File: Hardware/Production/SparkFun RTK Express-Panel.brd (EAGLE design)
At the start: 219.3 x 141.9 mm, 489 parts, among them J13 Internal, J16 microSD, J17 Qwiic Right Angle, J19 FPC_12_0.5MM_BACKFLIP, J20 External, J21 USB Female Type C Connector, J24 USB Female Type C Connector, J3 USB Female Type C Connector, J31 microSD, J33 Qwiic Right Angle, J34 Internal, J37 FPC_12_0.5MM_BACKFLIP, J39 External, J4 External, J40 USB Female Type C Connector, J43 USB Female Type C Connector, J5 USB Female Type C Connector, J50 microSD, J52 Qwiic Right Angle, J53 Internal, J56 FPC_12_0.5MM_BACKFLIP, Q1 SIL2308-TP, Q2 MBT3904DW1T1, Q3 MBT3904DW1T1, Q4 SIL2308-TP, Q5 MBT3904DW1T1, Q6 SIL2308-TP, U1 74HC4052D, U10 MCP73833, U11 CH340C, U12 MAX17048, U13 LIS2DH12, U14 ADP160, U15 MCP73833, U16 74HC4052D, U17 LIS2DH12, U18 ESP-WROOM-3232D-NARROW, U19 AP2112K-3.3, U2 AP2112K-3.3, U20 U-BLOX_ZED-F9P, U21 CH340C, U22 MAX17048, U23 ADP160, U24 MCP73833, U25 74HC4052D, U26 LIS2DH12, U27 ESP-WROOM-3232D-NARROW, U3 U-BLOX_ZED-F9P, U4 ADP160, U5 ESP-WROOM-3232D-NARROW, U6 CH340C, U7 MAX17048, U8 AP2112K-3.3, U9 U-BLOX_ZED-F9P

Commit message: Update v12 panel files.
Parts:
- added D19: 250mA/100V, SparkFun-DiscreteSemi:SOD-323
- added D20: 3A/10V/280mV, SparkFun-DiscreteSemi:SOD-323
- added D21: PESD0402, New_Parts:0402
- added U$184: (no value), output:L1#L20
- added U$185: (no value), output:ACTIVE1
- added U$186: (no value), output:ANTENNA2
- D10: value PRTR5V0U2F -> PESD0402; device SparkFun-IC-Power:SOT886 -> New_Parts:0402
- D11: value 250mA/100V -> PRTR5V0U2F; device SparkFun-DiscreteSemi:SOD-323 -> SparkFun-IC-Power:SOT886
- D12: value 3A/10V/280mV -> 250mA/100V
- D13, D16: value PRTR5V0U2F -> 3A/10V/280mV; device SparkFun-IC-Power:SOT886 -> SparkFun-DiscreteSemi:SOD-323
- D14: value 3A/10V/280mV -> PESD0402; device SparkFun-DiscreteSemi:SOD-323 -> New_Parts:0402
- D15, D18: value 3A/10V/280mV -> PRTR5V0U2F; device SparkFun-DiscreteSemi:SOD-323 -> SparkFun-IC-Power:SOT886
- D17: value 250mA/100V -> 3A/10V/280mV
- J19: value FPC_12_0.5MM_BACKFLIP -> External; device RTK Facet:FPC_12_DOUBLESIDED_BACKFLIP -> SparkFun-Connectors:JST04_1MM_RA
- J20: value External -> FPC_12_0.5MM_BACKFLIP; device SparkFun-Connectors:JST04_1MM_RA -> RTK Facet:FPC_12_DOUBLESIDED_BACKFLIP
- J37, J56: value FPC_12_0.5MM_BACKFLIP -> (none); device RTK Facet:FPC_12_DOUBLESIDED_BACKFLIP -> SparkFun-Connectors:1X01_NO_SILK
- J38, J57: value (none) -> FPC_12_0.5MM_BACKFLIP; device SparkFun-Connectors:1X01_NO_SILK -> RTK Facet:FPC_12_DOUBLESIDED_BACKFLIP
- U$100, U$161: device output:#ESP_RST#0 -> output:RTK0
- U$101, U$163: device output:RTK0 -> output:#GND#2
- U$102: device output:RTK0 -> output:#3V3#2
- U$103: device output:#GND#2 -> output:#SCL#1
- U$104: device output:#3V3#2 -> output:#SDA#0
- U$105: device output:#SCL#1 -> output:#D_SEL#0
- U$106: device output:#SDA#0 -> SparkFun-Aesthetics:QWIIC_4MM
- U$107: device output:#D_SEL#0 -> output:#TX_RDY#0
- U$108: device SparkFun-Aesthetics:QWIIC_4MM -> output:POWER0
- U$109: device output:#TX_RDY#0 -> output:CHG2
- U$110: device output:POWER0 -> output:GND3
- U$111: device output:CHG2 -> output:PWR0
- U$112: device output:GND3 -> output:SETUP1
- U$113: device output:PWR0 -> output:EXPRESS0
- U$114, U$175: device output:SETUP1 -> output:EXPRESS0
- U$115, U$177: device output:EXPRESS0 -> output:X0
- U$116: device output:EXPRESS0 -> output:Y1
- U$117: device output:X0 -> output:Z2
- U$118: device output:Y1 -> output:INT0
- U$119: device output:Z2 -> output:PWR_BTN1
- U$12: device output:#3V3#0 -> output:V120
- U$120: device output:V110 -> output:V120
- U$121: device output:INT0 -> output:OVERLAY0
- U$122: device output:PWR_BTN1 -> output:L1#L20
- U$123: device SparkFun-Aesthetics:QWIIC_4MM -> output:ACTIVE1
- U$124: device output:#3V3#0 -> output:ANTENNA2
- U$125: device output:#GND#0 -> SparkFun-Aesthetics:QWIIC_4MM
- U$126: device output:ANTENNA0 -> output:#3V3#0
- U$127: device output:#RTK#1 -> output:#GND#0
- U$128: device output:ACTIVE0 -> output:#RTK#1
- U$129: device output:L1#L21 -> SparkFun GPS RTK Surveyor:1553DBK-ENCLOSURE
- U$13: device output:#GND#0 -> output:ACTIVE1
- U$130: device SparkFun GPS RTK Surveyor:1553DBK-ENCLOSURE -> output:LIPO0
- U$131: device output:LIPO0 -> output:U#BLOX0
- U$132: device output:U#BLOX0 -> output:USB1
- U$133: device output:USB1 -> output:SERIAL20
- U$134: device output:SERIAL20 -> output:SERIAL10
- U$135: device output:SERIAL10 -> output:#RX2#2
- U$136: device output:#RX2#2 -> output:#TX2#1
- U$137: device output:#TX2#1 -> output:#RX1#2
- U$138: device output:#RX1#2 -> output:#TX1#1
- U$139: device output:#TX1#1 -> output:#3V3#0
- U$140, U$64: device output:#3V3#0 -> output:#GND#0
- U$142, U$69: device output:#GND#0 -> output:NMEA1
- U$143: device output:NMEA1 -> output:RADIO0
- U$144: device output:RADIO0 -> output:##RST##4
- U$145: device output:##RST##4 -> output:##SAFE##5
- U$146: device output:##SAFE##5 -> output:#FENCE#3
- U$147: device output:#FENCE#3 -> output:#3#5#5V#0
- U$148: device output:#3#5#5V#0 -> output:#PPS#0
- U$149: device output:#PPS#0 -> output:#RX#2
- U$15: device output:ANTENNA0 -> output:ANTENNA2
- U$150: device output:#RX#2 -> output:ZED0
- U$151: device output:ZED0 -> output:#TX#1
- U$152: device output:#TX#1 -> output:USB1
- U$153: device output:USB1 -> output:ESP320
- U$154: device output:ESP320 -> output:#3V3#0
- U$155: device output:#3V3#0 -> output:#TX1#1
- U$156: device output:#TX1#1 -> output:#RX1#2
- U$157: device output:#RX1#2 -> output:#GND#0
- U$158: device output:#GND#0 -> output:MICROSD0
- U$159: device output:MICROSD0 -> output:#GND#1
- U$160: device output:#GND#1 -> output:#ESP_RST#0
- U$164: device output:#GND#2 -> output:#3V3#2
- U$165: device output:#3V3#2 -> output:#SCL#1
- U$166: device output:#SCL#1 -> output:#SDA#0
- U$167: device output:#SDA#0 -> output:#D_SEL#0
- U$168: device output:#D_SEL#0 -> SparkFun-Aesthetics:QWIIC_4MM
- U$169: device SparkFun-Aesthetics:QWIIC_4MM -> output:#TX_RDY#0
- U$170: device output:#TX_RDY#0 -> output:POWER0
- U$171: device output:POWER0 -> output:CHG2
- U$172: device output:CHG2 -> output:GND3
- U$173: device output:GND3 -> output:PWR0
- U$174: device output:PWR0 -> output:SETUP1
- U$178: device output:X0 -> output:Y1
- U$179: device output:Y1 -> output:Z2
- U$18: device output:ACTIVE0 -> output:#3V3#0
- U$180: device output:Z2 -> output:INT0
- U$181: device output:V110 -> output:PWR_BTN1
- U$182: device output:INT0 -> output:V120
- U$183: device output:PWR_BTN1 -> output:OVERLAY0
- U$19: device output:L1#L21 -> output:#GND#0
- U$21: device output:ACTIVE0 -> SparkFun GPS RTK Surveyor:1553DBK-ENCLOSURE
- U$22: device output:L1#L21 -> output:LIPO0
- U$25: device SparkFun GPS RTK Surveyor:1553DBK-ENCLOSURE -> output:U#BLOX0
- U$44: device output:LIPO0 -> output:USB1
- U$52: device output:U#BLOX0 -> output:SERIAL20
- U$54: device output:USB1 -> output:SERIAL10
- U$57: device output:SERIAL20 -> output:#RX2#2
- U$58: device output:SERIAL10 -> output:#TX2#1
- U$59: device output:#RX2#2 -> output:#RX1#2
- U$6: device output:ANTENNA0 -> output:L1#L20
- U$61: device output:#TX2#1 -> output:#TX1#1
- U$62: device output:#RX1#2 -> output:#3V3#0
- U$63, U$95: device output:#TX1#1 -> output:#GND#0
- U$71: device output:#GND#0 -> output:RADIO0
- U$73: device output:NMEA1 -> output:##RST##4
- U$75: device output:RADIO0 -> output:##SAFE##5
- U$76: device output:##RST##4 -> output:#FENCE#3
- U$77: device output:##SAFE##5 -> output:#3#5#5V#0
- U$78: device output:#FENCE#3 -> output:#PPS#0
- U$79: device output:#3#5#5V#0 -> output:#RX#2
- U$8: device output:V110 -> output:OVERLAY0
- U$80: device output:#PPS#0 -> output:ZED0
- U$81: device output:#RX#2 -> output:#TX#1
- U$89: device output:ZED0 -> output:USB1
- U$90: device output:#TX#1 -> output:ESP320
- U$91: device output:USB1 -> output:#3V3#0
- U$92: device output:ESP320 -> output:#TX1#1
- U$94: device output:#3V3#0 -> output:#RX1#2
- U$96: device output:#RX1#2 -> output:MICROSD0
- U$97: device output:#GND#0 -> output:#GND#1
- U$98: device output:MICROSD0 -> output:#ESP_RST#0
- U$99: device output:#GND#1 -> output:RTK0
- U14, U23, U4: value ADP160 -> STLQ015-3.3V
- moved J19 113.9 mm to (102.9, 4.74), flipped to the bottom
- moved D14 113.0 mm to (90.9, 10.3), flipped to the top, turned to 180 degrees
- moved U$12 110.0 mm to (34.2, 97.3)
- moved J20 105.1 mm to (51.2, 96.3), flipped to the top, turned to 180 degrees
- moved U$18 104.7 mm to (122.4, 31.7)
- moved U$19 103.0 mm to (122.6, 24.1)
- moved U$124 101.7 mm to (91.3, 12.3)
- moved U$13 100.5 mm to (22.6, 13.8)
- moved U$44 92.9 mm to (100.8, 7.03)
- moved D10 92.8 mm to (22.2, 10.3), turned to 180 degrees
- moved U$131 91.3 mm to (168.7, 8.43)
- moved D16 88.1 mm to (160.6, 99.3), flipped to the bottom
- moved U$22 84.5 mm to (81.4, 97.9)
- moved U$98 83.2 mm to (130.8, 98.0), turned to 0 degrees
- moved U$159 80.7 mm to (199.5, 95.4), turned to 0 degrees
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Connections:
- net 3.3V1: now also J19.2; no longer J20.2
- net CHG_LED_RES: now also J20.3, J20.4; no longer J19.10, J19.9
- net CHG_LED_RES1: now also J38.3, J38.4; no longer J37.10, J37.9
- net CHG_LED_RES2: now also J57.3, J57.4; no longer J56.10, J56.9
- net D+3: now also D11.4; no longer D10.4
- net D+4: now also D15.4; no longer D13.4
- net D+5: now also D18.4; no longer D16.4
- net D-3: now also D11.6; no longer D10.6
- net D-4: now also D15.6; no longer D13.6
- net D-5: now also D18.6; no longer D16.6
- net ESP_13/POWER_CTRL1: now also D12.A; no longer D11.A
- net ESP_13/POWER_CTRL2: now also D19.A; no longer D17.A
- net ESP_14/SETUP_BUTTON: now also J20.7, J20.8; no longer J19.5, J19.6
- net ESP_14/SETUP_BUTTON1: now also J38.7, J38.8; no longer J37.5, J37.6
- net ESP_14/SETUP_BUTTON2: now also J57.7, J57.8; no longer J56.5, J56.6
- net ESP_21/SDA1: now also J19.3; no longer J20.3
- net ESP_22/SCL1: now also J19.4; no longer J20.4
- net ESP_4/ACCEL_INT1: now also J37.1; no longer J38.1
- net ESP_4/ACCEL_INT2: now also J56.1; no longer J57.1
- net ESP_D1+1: now also D11.3; no longer D10.3
- net ESP_D1+2: now also D18.3; no longer D16.3
- net ESP_D1-1: now also D11.1; no longer D10.1
- net ESP_D1-2: now also D18.1; no longer D16.1
- net GND: now also D10.2, J20.11, J20.12; no longer J19.1, J19.2
- net GND1: now also D11.2, D14.2, J19.1, J38.11, J38.12; no longer D10.2, J20.1, J37.1, J37.2
- net GND2: now also D15.2, D18.2, D21.2, J57.11, J57.12; no longer D13.2, D16.2, J56.1, J56.2
- net GPS_ANT1: now also D10.1
- net GPS_ANT2: now also D14.1
- net GPS_ANT3: now also D21.1
- net N$23: now also D17.A; no longer D15.A
- net POWER_BTN: now also J20.10, J20.9; no longer J19.3, J19.4
- net POWER_BTN1: now also D12.C, J38.10, J38.9; no longer D11.C, J37.3, J37.4
- net POWER_BTN2: now also D19.C, J57.10, J57.9; no longer D17.C, J56.3, J56.4
- net UNP_D+2: now also D15.3; no longer D13.3
- net UNP_D-2: now also D15.1; no longer D13.1
- net VOUT: now also J11.4, J9.1
- net VOUT1: now also J25.1, J27.4
- net VOUT2: now also J44.1, J46.4
- net V_BATT2: now also D16.A; no longer D14.A
- net V_RAW: no longer J11.4, J9.1
- net V_RAW1: now also D13.C; no longer D12.C, J25.1, J27.4
- net V_RAW2: now also D16.C, D20.C; no longer D14.C, D18.C, J44.1, J46.4
- net V_USB: now also J20.1, J20.2; no longer J19.11, J19.12
- net V_USB1: now also D11.5, D13.A, J38.1, J38.2; no longer D10.5, D12.A, J37.11, J37.12
- net V_USB2: now also D15.5, D17.C, D18.5, D20.A, J57.1, J57.2; no longer D13.5, D15.C, D16.5, D18.A, J56.11, J56.12
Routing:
- net VOUT2: track 12.9 -> 80.8 mm, vias 0 -> 2
- net VOUT1: track 12.9 -> 80.8 mm, vias 0 -> 2
- net VOUT: track 12.9 -> 80.8 mm, vias 0 -> 2
- net V_RAW: track 148.6 -> 104.2 mm
- net V_RAW2: track 148.6 -> 104.2 mm
- net V_RAW1: track 148.6 -> 104.2 mm
- net CHG_LED_RES1: track 44.7 -> 26.4 mm
- net CHG_LED_RES: track 44.7 -> 26.4 mm
- net CHG_LED_RES2: track 44.7 -> 26.4 mm
- net POWER_BTN2: track 157.1 -> 143.0 mm, vias 3 -> 4
- net POWER_BTN1: track 157.1 -> 143.0 mm, vias 3 -> 4
- net POWER_BTN: track 157.1 -> 143.0 mm, vias 3 -> 4
- net ESP_14/SETUP_BUTTON1: track 45.6 -> 31.7 mm
- net ESP_14/SETUP_BUTTON2: track 45.6 -> 31.7 mm
- net ESP_14/SETUP_BUTTON: track 45.6 -> 31.7 mm
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
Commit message: v13 PCB. Add panel. Change from SMD SMA To edge mount SMD to increase strength of connector.
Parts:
- D10, D14, D21: device New_Parts:0402 -> SparkFun-DiscreteSemi:0402
- E1, E2, E3: device SparkFun-RF:SMA-EDGE-SMD -> SparkFun-RF:SMA-EDGE
- J20, J38, J57: value FPC_12_0.5MM_BACKFLIP -> (none)
- U$12: device output:V120 -> output:#3V3#0
- U$120, U$182: device output:V120 -> output:OVERLAY0
- U$121, U$183: device output:OVERLAY0 -> output:L1#L20
- U$122, U$184: device output:L1#L20 -> output:ACTIVE1
- U$123, U$185: device output:ACTIVE1 -> output:ANTENNA2
- U$124, U$186: device output:ANTENNA2 -> output:V130
- U$18: device output:#3V3#0 -> output:V130
- moved U$18 110.0 mm to (34.1, 97.3)
- moved U$12 110.0 mm to (122.4, 31.7)
- moved U$121 89.7 mm to (91.3, 15.3)
- moved U$183 89.7 mm to (160.0, 15.3)
- moved U$124 85.8 mm to (102.8, 97.3)
- moved U$186 85.8 mm to (171.5, 97.3)
- moved U$120 17.3 mm to (119.9, 100.3)
- moved U$182 17.3 mm to (188.6, 100.3)
- moved E1 3.56 mm to (22.7, 3.60)
- moved E2 3.56 mm to (91.4, 3.60)
- moved E3 3.56 mm to (160.1, 3.60)
- moved U$122 1.50 mm to (91.3, 13.8)
- moved U$123 1.50 mm to (91.3, 12.3)
- moved U$184 1.50 mm to (160.0, 13.8)
- moved U$185 1.50 mm to (160.0, 12.3)
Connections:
- net GND: now also E1.GND@2, E1.GND@3
- net GND1: now also E2.GND@2, E2.GND@3
- net GND2: now also E3.GND@2, E3.GND@3
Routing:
- net GPS_ANT2: track 15.9 -> 24.9 mm
- net GPS_ANT3: track 15.9 -> 24.9 mm
- net GPS_ANT1: track 15.9 -> 24.9 mm
- net GND2: vias 205 -> 201
- net GND1: vias 205 -> 201
- net GND: vias 205 -> 201
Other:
- outline, holes or cut-outs redrawn

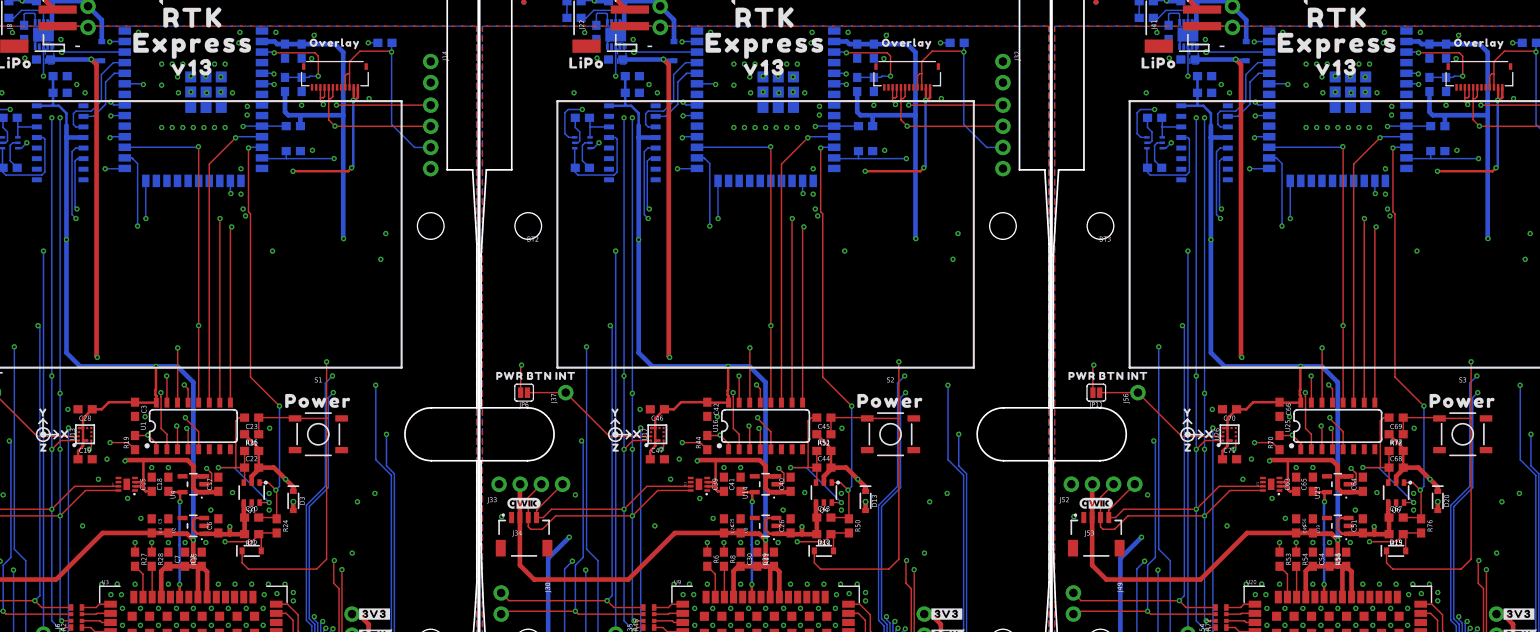
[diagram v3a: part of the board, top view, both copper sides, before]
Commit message: v14 - Remove ground plane from around accelerometer
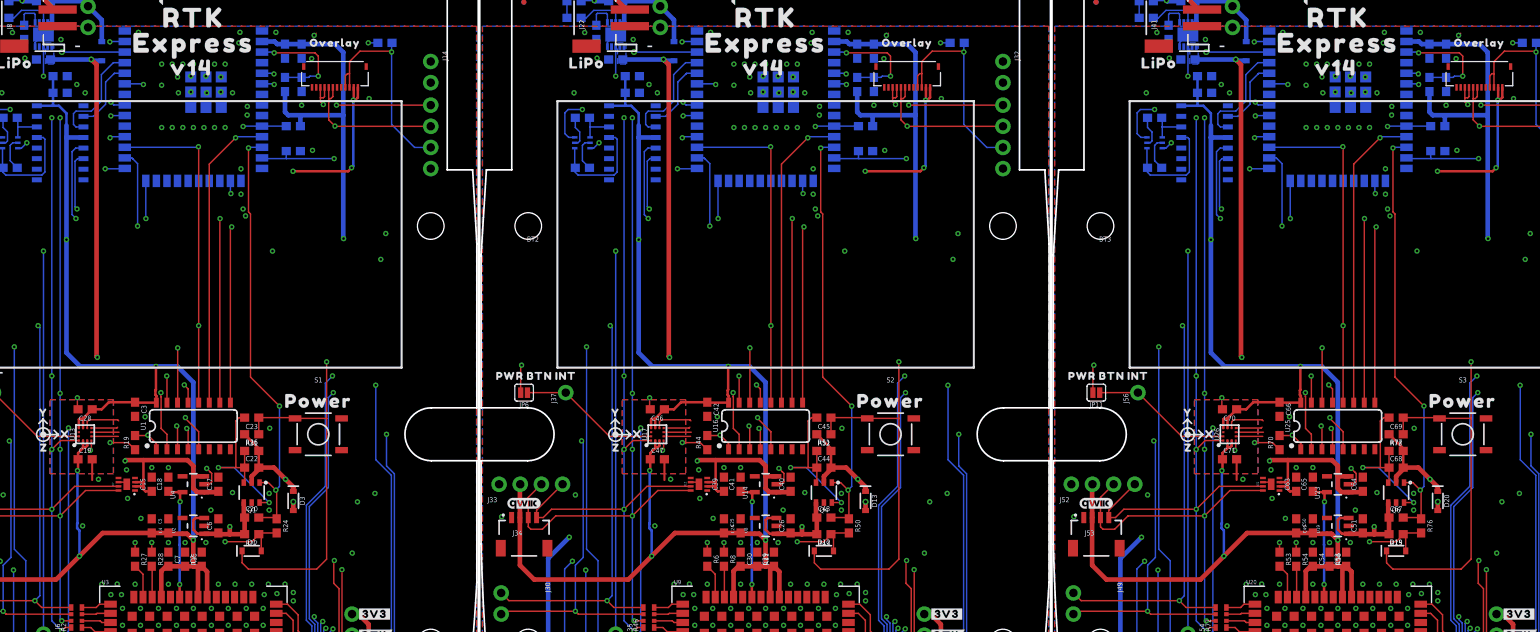
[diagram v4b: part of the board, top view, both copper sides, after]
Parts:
- U$12: device output:#3V3#0 -> output:V140
- U$124, U$186: device output:V130 -> output:V140
- U$18: device output:V130 -> output:#3V3#0
- moved U$12 110.1 mm to (34.0, 97.3)
- moved U$18 110.0 mm to (122.4, 31.7)
- moved U$124 0.13 mm to (102.7, 97.3)
- moved U$186 0.13 mm to (171.4, 97.3)
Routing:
- net GND2: track 18.1 -> 37.5 mm
- net GND1: track 18.1 -> 37.5 mm
- net GND: track 18.1 -> 37.5 mm
- net 3.3V1: track 317.2 -> 329.2 mm, vias 6 -> 8
- net 3.3V: track 317.2 -> 329.2 mm, vias 6 -> 8
- net 3.3V2: track 317.2 -> 329.2 mm, vias 6 -> 8
